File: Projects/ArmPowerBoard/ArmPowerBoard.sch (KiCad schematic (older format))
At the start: 5 parts

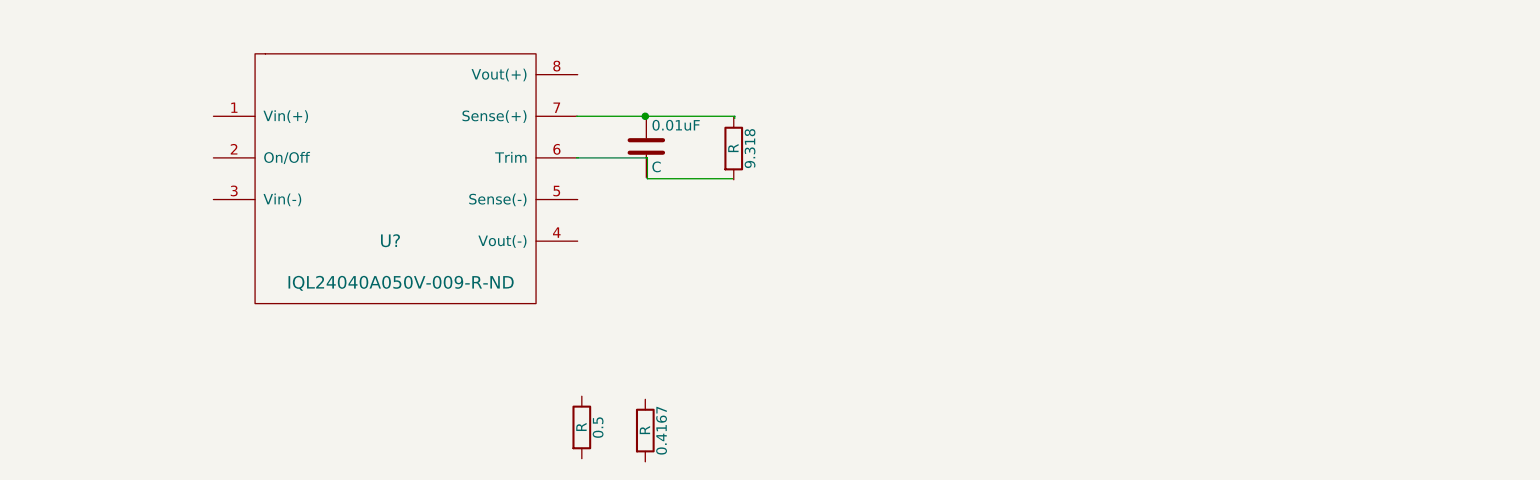
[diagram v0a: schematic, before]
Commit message: Edit Arm power board
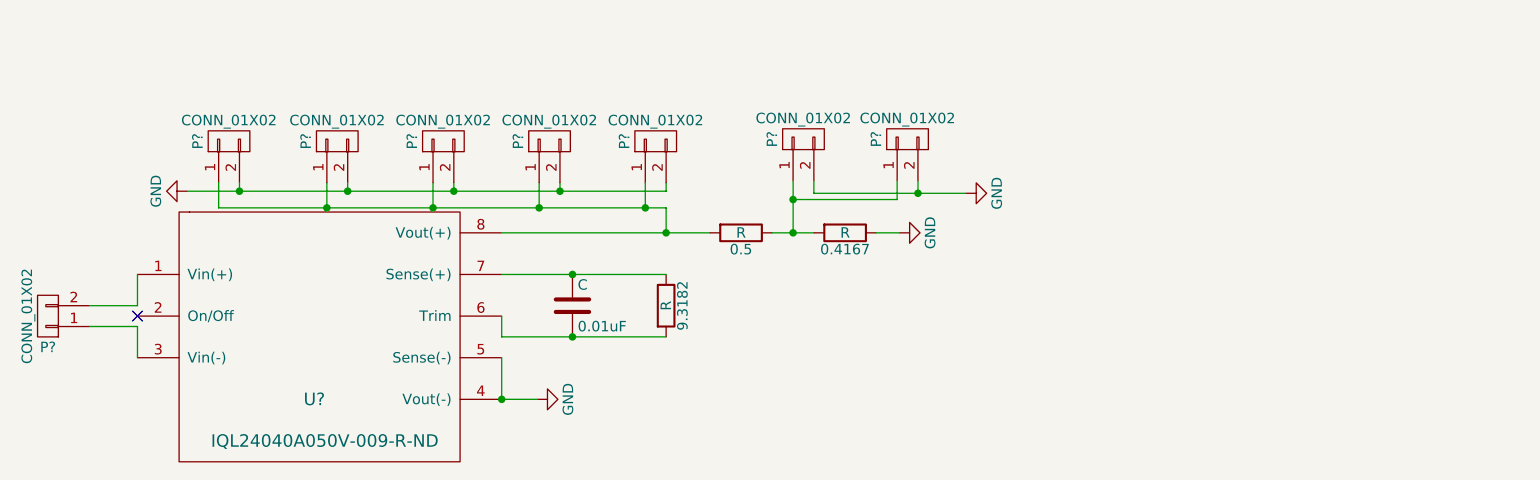
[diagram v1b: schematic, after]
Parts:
- removed 0.01uF: C, symbol C
- removed 9.318: R, symbol R
- removed U?: IQL24040A050V-009-R-ND, symbol IQL24040A050V-009-R-ND
- added 9.3182: R, symbol R
- added C: 0.01uF, symbol C
- added P? (x8): CONN_01X02, symbol CONN_01X02
- added U?: IQL24040A050V-009-R-ND, symbol IQL24040A050V-009-R-ND
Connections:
- net labels added: GND
- wire segments 6 -> 31
- no-connect marks 0 -> 1

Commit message: did some work on the ArmPowerBoard schematic and layout
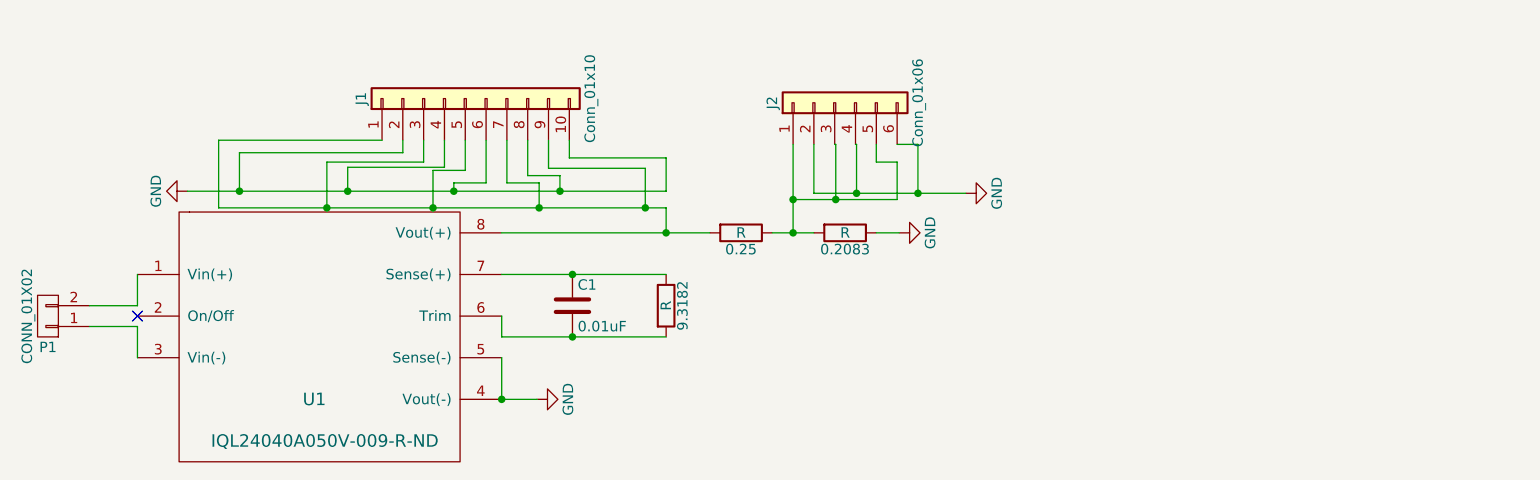
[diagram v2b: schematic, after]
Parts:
- removed P? (x7): CONN_01X02, symbol CONN_01X02
- added J1: Conn_01x10, USST-footprints:Phoenix_Contact_Terminal_Block_1x10_1935242, symbol Conn_01x10
- added J2: Conn_01x06, USST-footprints:TerminalBlock_Pheonix_PT-5mm_6pol, symbol Conn_01x06
- 0.2083: renamed from 0.4167; footprint (none) -> Resistors_SMD:R_1218
- 0.25: renamed from 0.5; footprint (none) -> Resistors_SMD:R_1218
- 9.3182: footprint (none) -> Resistors_SMD:R_1218
- C1: renamed from C; footprint (none) -> Capacitors_SMD:C_1206
- P1: renamed from P?; footprint (none) -> USST-footprints:Phoenix_Contact_1770539
- U1: renamed from U?; footprint (none) -> USST-footprints:IQL24040A050V_Power_Supply
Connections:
- net GND: now also J1.10 (Pin_10), J1.2 (Pin_2), J1.4 (Pin_4), J1.6 (Pin_6), J1.8 (Pin_8), J2.2 (Pin_2), J2.4 (Pin_4), J2.6 (Pin_6)
- net at 0.25.2, U1.8 (Vout(+)): now also J1.1 (Pin_1), J1.3 (Pin_3), J1.5 (Pin_5), J1.7 (Pin_7), J1.9 (Pin_9)
- net at 0.2083.2, 0.25.1: now also J2.1 (Pin_1), J2.3 (Pin_3), J2.5 (Pin_5)
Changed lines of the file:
@@
 LIBS:contrib
 LIBS:valves
-LIBS:USST-parts
 LIBS:ArmPowerBoard-cache
 EELAYER 25 0
@@
 NoConn ~ 3650 3220
 $Comp
-L IQL24040A050V-009-R-ND U?
+L IQL24040A050V-009-R-ND U1
 U 1 1 5AC545D9
 P 4500 3520
-F 0 "U?" H 4500 3420 60  0000 C CNN
+F 0 "U1" H 4500 3420 60  0000 C CNN
 F 1 "IQL24040A050V-009-R-ND" H 4550 3220 60  0000 C CNN
-F 2 "" H 4400 3420 60  0001 C CNN
+F 2 "USST-footprints:IQL24040A050V_Power_Supply" H 4400 3420 60  0001 C CNN
 F 3 "" H 4400 3420 60  0001 C CNN
 	1    4500 3520
@@
 $EndComp
 $Comp
-L C C
+L C C1
 U 1 1 5AC54A7E
 P 5740 3170
-F 0 "C" H 5765 3270 50  0000 L CNN
+F 0 "C1" H 5765 3270 50  0000 L CNN
 F 1 "0.01uF" H 5765 3070 50  0000 L CNN
-F 2 "" H 5778 3020 50  0000 C CNN
+F 2 "Capacitors_SMD:C_1206" H 5778 3020 50  0001 C CNN
 F 3 "" H 5740 3170 50  0000 C CNN
 	1    5740 3170
@@
 F 0 "9.3182" V 6270 3170 50  0000 C CNN
 F 1 "R" V 6190 3170 50  0000 C CNN
-F 2 "" V 6120 3170 50  0000 C CNN
+F 2 "Resistors_SMD:R_1218" V 6120 3170 50  0001 C CNN
 F 3 "" H 6190 3170 50  0000 C CNN
 	1    6190 3170
@@
 $EndComp
 $Comp
-L R 0.4167
+L R 0.2083
 U 1 1 5AC54C78
 P 7050 2820
-F 0 "0.4167" V 7130 2820 50  0000 C CNN
+F 0 "0.2083" V 7130 2820 50  0000 C CNN
 F 1 "R" V 7050 2820 50  0000 C CNN
-F 2 "" V 6980 2820 50  0000 C CNN
+F 2 "Resistors_SMD:R_1218" V 6980 2820 50  0001 C CNN
 F 3 "" H 7050 2820 50  0000 C CNN
 	1    7050 2820
@@
 $EndComp
 $Comp
-L R 0.5
+L R 0.25
 U 1 1 5AC54CA5
 P 6550 2820
-F 0 "0.5" V 6630 2820 50  0000 C CNN
+F 0 "0.25" V 6630 2820 50  0000 C CNN
 F 1 "R" V 6550 2820 50  0000 C CNN
-F 2 "" V 6480 2820 50  0000 C CNN
+F 2 "Resistors_SMD:R_1218" V 6480 2820 50  0001 C CNN
 F 3 "" H 6550 2820 50  0000 C CNN
 	1    6550 2820
@@
 $EndComp
 $Comp
-L GND #PWR?
+L GND #PWR01
 U 1 1 5AC54E0F
 P 7310 2820
-F 0 "#PWR?" H 7310 2570 50  0001 C CNN
+F 0 "#PWR01" H 7310 2570 50  0001 C CNN
 F 1 "GND" H 7310 2670 50  0000 C CNN
 F 2 "" H 7310 2820 50  0000 C CNN
@@
 $EndComp
 $Comp
-L GND #PWR?
+L GND #PWR02
 U 1 1 5AC55060
 P 5570 3620
-F 0 "#PWR?" H 5570 3370 50  0001 C CNN
+F 0 "#PWR02" H 5570 3370 50  0001 C CNN
 F 1 "GND" H 5570 3470 50  0000 C CNN
 F 2 "" H 5570 3620 50  0000 C CNN
@@
 $EndComp
 $Comp
-L CONN_01X02 P?
+L CONN_01X02 P1
 U 1 1 5AC864F2
 P 3220 3220
-F 0 "P?" H 3220 3370 50  0000 C CNN
+F 0 "P1" H 3220 3370 50  0000 C CNN
 F 1 "CONN_01X02" V 3320 3220 50  0000 C CNN
-F 2 "" H 3220 3220 50  0000 C CNN
+F 2 "USST-footprints:Phoenix_Contact_1770539" H 3220 3220 50  0001 C CNN
 F 3 "" H 3220 3220 50  0000 C CNN
 	1    3220 3220
@@
 $EndComp
 $Comp
-L CONN_01X02 P?
-U 1 1 5AC86753
-P 6140 2380
-F 0 "P?" H 6140 2530 50  0000 C CNN
-F 1 "CONN_01X02" V 6240 2380 50  0000 C CNN
-F 2 "" H 6140 2380 50  0000 C CNN
-F 3 "" H 6140 2380 50  0000 C CNN
-	1    6140 2380
-	0    -1   -1   0
-$EndComp
-$Comp
-L CONN_01X02 P?
-U 1 1 5AC867AF
-P 5630 2380
-F 0 "P?" H 5630 2530 50  0000 C CNN
-F 1 "CONN_01X02" V 5730 2380 50  0000 C CNN
-F 2 "" H 5630 2380 50  0000 C CNN
-F 3 "" H 5630 2380 50  0000 C CNN
-	1    5630 2380
-	0    -1   -1   0
-$EndComp
-$Comp
-L CONN_01X02 P?
-U 1 1 5AC867D8
-P 5120 2380
-F 0 "P?" H 5120 2530 50  0000 C CNN
-F 1 "CONN_01X02" V 5220 2380 50  0000 C CNN
-F 2 "" H 5120 2380 50  0000 C CNN
-F 3 "" H 5120 2380 50  0000 C CNN
-	1    5120 2380
-	0    -1   -1   0
-$EndComp
-$Comp
-L CONN_01X02 P?
-U 1 1 5AC86811
-P 4610 2380
-F 0 "P?" H 4610 2530 50  0000 C CNN
-F 1 "CONN_01X02" V 4710 2380 50  0000 C CNN
-F 2 "" H 4610 2380 50  0000 C CNN
-F 3 "" H 4610 2380 50  0000 C CNN
-	1    4610 2380
-	0    -1   -1   0
-$EndComp
-$Comp
-L CONN_01X02 P?
-U 1 1 5AC86844
-P 4090 2380
-F 0 "P?" H 4090 2530 50  0000 C CNN
-F 1 "CONN_01X02" V 4190 2380 50  0000 C CNN
-F 2 "" H 4090 2380 50  0000 C CNN
-F 3 "" H 4090 2380 50  0000 C CNN
-	1    4090 2380
-	0    -1   -1   0
-$EndComp
-$Comp
-L GND #PWR?
+L GND #PWR03
 U 1 1 5AC86D1C
 P 3890 2620
-F 0 "#PWR?" H 3890 2370 50  0001 C CNN
+F 0 "#PWR03" H 3890 2370 50  0001 C CNN
 F 1 "GND" H 3890 2470 50  0000 C CNN
 F 2 "" H 3890 2620 50  0000 C CNN
@@
 	0    1    1    0
 $EndComp
-Wire Wire Line
-	6190 3020 5400 3020
-Wire Wire Line
-	5400 3220 5400 3320
-Wire Wire Line
-	5400 3320 6190 3320
-Connection ~ 5740 3020
-Connection ~ 5740 3320
-Wire Wire Line
-	5400 2820 6400 2820
-Wire Wire Line
-	6700 2820 6900 2820
-Wire Wire Line
-	7200 2820 7310 2820
-Connection ~ 6190 2820
-Wire Wire Line
-	6800 2570 6800 2820
-Connection ~ 6800 2820
-Wire Wire Line
-	5400 3420 5400 3620
-Wire Wire Line
-	5390 3620 5570 3620
-Connection ~ 5400 3620
-Wire Wire Line
-	3650 3170 3650 3020
-Wire Wire Line
-	3420 3170 3650 3170
-Wire Wire Line
-	3420 3270 3650 3270
-Wire Wire Line
-	3650 3270 3650 3420
-Wire Wire Line
-	6190 2620 6190 2580
-Wire Wire Line
-	3890 2620 6190 2620
-Wire Wire Line
-	4660 2580 4660 2620
-Connection ~ 4660 2620
-Wire Wire Line
-	4140 2580 4140 2620
-Connection ~ 4140 2620
-Wire Wire Line
-	5170 2580 5170 2620
-Connection ~ 5170 2620
-Wire Wire Line
-	5680 2580 5680 2620
-Connection ~ 5680 2620
-Wire Wire Line
-	4040 2580 4040 2700
-Wire Wire Line
-	4040 2700 6190 2700
-Wire Wire Line
-	6190 2700 6190 2820
-Wire Wire Line
-	4560 2580 4560 2700
-Connection ~ 4560 2700
-Wire Wire Line
-	5070 2580 5070 2700
-Connection ~ 5070 2700
-Wire Wire Line
-	5580 2580 5580 2700
-Connection ~ 5580 2700
-Wire Wire Line
-	6090 2580 6090 2700
-Connection ~ 6090 2700
-$Comp
-L CONN_01X02 P?
-U 1 1 5AC879B1
-P 6850 2370
-F 0 "P?" H 6850 2520 50  0000 C CNN
-F 1 "CONN_01X02" V 6950 2370 50  0000 C CNN
-F 2 "" H 6850 2370 50  0000 C CNN
-F 3 "" H 6850 2370 50  0000 C CNN
-	1    6850 2370
-	0    -1   -1   0
-$EndComp
-$Comp
-L CONN_01X02 P?
-U 1 1 5AC879EA
-P 7350 2370
-F 0 "P?" H 7350 2520 50  0000 C CNN
-F 1 "CONN_01X02" V 7450 2370 50  0000 C CNN
-F 2 "" H 7350 2370 50  0000 C CNN
-F 3 "" H 7350 2370 50  0000 C CNN
-	1    7350 2370
-	0    -1   -1   0
-$EndComp
-Wire Wire Line
-	6800 2660 7300 2660
-Wire Wire Line
-	7300 2660 7300 2570
-Connection ~ 6800 2660
-Wire Wire Line
-	6900 2570 6900 2630
-Wire Wire Line
-	6900 2630 7630 2630
-Wire Wire Line
-	7400 2570 7400 2630
-Connection ~ 7400 2630
-$Comp
-L GND #PWR?
+$Comp
+L GND #PWR04
 U 1 1 5AC87C8C
 P 7630 2630
-F 0 "#PWR?" H 7630 2380 50  0001 C CNN
+F 0 "#PWR04" H 7630 2380 50  0001 C CNN
 F 1 "GND" H 7630 2480 50  0000 C CNN
 F 2 "" H 7630 2630 50  0000 C CNN
@@
 	0    -1   -1   0
 $EndComp
+$Comp
+L Conn_01x06 J2
+U 1 1 5AC95135
+P 7000 2195
+F 0 "J2" H 7000 2495 50  0000 C CNN
+F 1 "Conn_01x06" H 7000 1795 50  0000 C CNN
+F 2 "USST-footprints:TerminalBlock_Pheonix_PT-5mm_6pol" H 7000 2195 50  0001 C CNN
+F 3 "" H 7000 2195 50  0001 C CNN
+	1    7000 2195
+	0    -1   -1   0
+$EndComp
+$Comp
+L Conn_01x10 J1
+U 1 1 5AC943C7
+P 5225 2175
+F 0 "J1" H 5225 2675 50  0000 C CNN
+F 1 "Conn_01x10" H 5225 1575 50  0000 C CNN
+F 2 "USST-footprints:Phoenix_Contact_Terminal_Block_1x10_1935242" H 5225 2175 50  0001 C CNN
+F 3 "" H 5225 2175 50  0001 C CNN
+	1    5225 2175
+	0    -1   -1   0
+$EndComp
+Wire Wire Line
+	5625 2510 5625 2375
+Wire Wire Line
+	6090 2510 5625 2510
+Wire Wire Line
+	5525 2545 5525 2375
+Wire Wire Line
+	5680 2545 5525 2545
+Wire Wire Line
+	5425 2580 5425 2375
+Wire Wire Line
+	5580 2580 5425 2580
+Wire Wire Line
+	5325 2580 5325 2375
+Wire Wire Line
+	5170 2580 5325 2580
+Wire Wire Line
+	5225 2520 5225 2375
+Wire Wire Line
+	5070 2520 5225 2520
+Wire Wire Line
+	5125 2505 5125 2375
+Wire Wire Line
+	4660 2505 5125 2505
+Wire Wire Line
+	5025 2480 5025 2375
+Wire Wire Line
+	4560 2480 5025 2480
+Connection ~ 7400 2630
+Wire Wire Line
+	7400 2395 7400 2630
+Wire Wire Line
+	6900 2630 7630 2630
+Wire Wire Line
+	6900 2395 6900 2630
+Connection ~ 6800 2660
+Wire Wire Line
+	7300 2480 7300 2660
+Wire Wire Line
+	7300 2660 6800 2660
+Connection ~ 6090 2700
+Wire Wire Line
+	6090 2510 6090 2700
+Connection ~ 5580 2700
+Wire Wire Line
+	5580 2580 5580 2700
+Connection ~ 5070 2700
+Wire Wire Line
+	5070 2520 5070 2700
+Connection ~ 4560 2700
+Wire Wire Line
+	4560 2480 4560 2700
+Wire Wire Line
+	6190 2700 6190 2820
+Wire Wire Line
+	4040 2700 6190 2700
+Connection ~ 5680 2620
+Wire Wire Line
+	5680 2545 5680 2620
+Connection ~ 5170 2620
+Wire Wire Line
+	5170 2580 5170 2620
+Connection ~ 4140 2620
+Connection ~ 4660 2620
+Wire Wire Line
+	4660 2505 4660 2620
+Wire Wire Line
+	6190 2620 3890 2620
+Wire Wire Line
+	6190 2460 6190 2620
+Wire Wire Line
+	3650 3270 3650 3420
+Wire Wire Line
+	3420 3270 3650 3270
+Wire Wire Line
+	3420 3170 3650 3170
+Wire Wire Line
+	3650 3170 3650 3020
+Wire Wire Line
+	5400 3420 5400 3620
+Connection ~ 6800 2820
+Wire Wire Line
+	6800 2395 6800 2820
+Connection ~ 6190 2820
+Wire Wire Line
+	7200 2820 7310 2820
+Wire Wire Line
+	6700 2820 6900 2820
+Wire Wire Line
+	5400 2820 6400 2820
+Connection ~ 5740 3320
+Connection ~ 5740 3020
+Wire Wire Line
+	5400 3320 6190 3320
+Wire Wire Line
+	5400 3220 5400 3320
+Wire Wire Line
+	6190 3020 5400 3020
+Wire Wire Line
+	6190 2460 5725 2460
+Wire Wire Line
+	5725 2460 5725 2375
+Wire Wire Line
+	7300 2480 7200 2480
+Wire Wire Line
+	7200 2480 7200 2395
+Connection ~ 7005 2660
+Wire Wire Line
+	7005 2660 7005 2395
+Wire Wire Line
+	7005 2395 7000 2395
+Connection ~ 7105 2630
+Wire Wire Line
+	7105 2630 7105 2395
+Wire Wire Line
+	7105 2395 7100 2395
+Wire Wire Line
+	7400 2395 7300 2395
+Wire Wire Line
+	4040 2700 4040 2375
+Wire Wire Line
+	4040 2375 4825 2375
+Wire Wire Line
+	4140 2620 4140 2435
+Wire Wire Line
+	4140 2435 4925 2435
+Wire Wire Line
+	4925 2435 4925 2375
+Connection ~ 5400 3620
+Wire Wire Line
+	5400 3620 5570 3620
 $EndSCHEMATC

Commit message: Made the Arm PCB
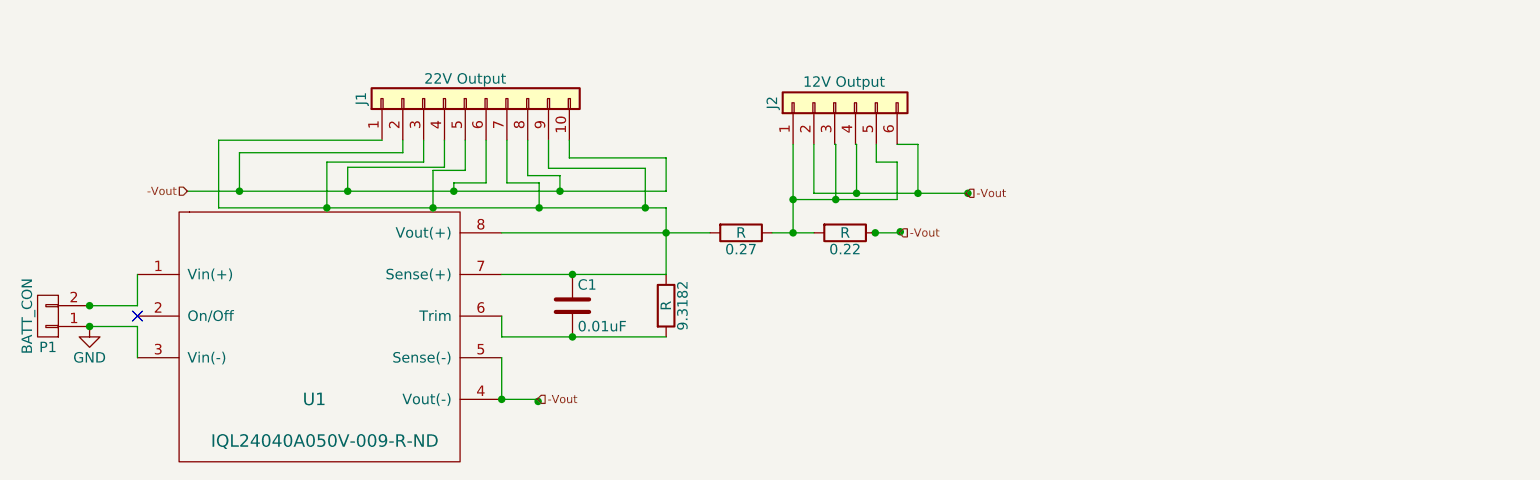
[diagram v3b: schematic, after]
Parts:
- J1: value Conn_01x10 -> 22V Output
- J2: value Conn_01x06 -> 12V Output
- P1: value CONN_01X02 -> BATT_CON
- renumbered 0.2083 to 0.22, 0.25 to 0.27
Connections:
- net GND: now also P1.1 (P1), U1.3 (Vin(-)); no longer 0.22.1, J1.10 (Pin_10), J1.2 (Pin_2), J1.4 (Pin_4), J1.6 (Pin_6), J1.8 (Pin_8), J2.2 (Pin_2), J2.4 (Pin_4), J2.6 (Pin_6), U1.4 (Vout(-)), U1.5 (Sense(-))
- net at 9.3182.1, C1.1, U1.7 (Sense(+)): now also 0.27.2, J1.1 (Pin_1), J1.3 (Pin_3), J1.5 (Pin_5), J1.7 (Pin_7), J1.9 (Pin_9), U1.8 (Vout(+))
- new net -Vout: 0.22.1, J1.10 (Pin_10), J1.2 (Pin_2), J1.4 (Pin_4), J1.6 (Pin_6), J1.8 (Pin_8), J2.2 (Pin_2), J2.4 (Pin_4), J2.6 (Pin_6), U1.4 (Vout(-)), U1.5 (Sense(-))
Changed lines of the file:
@@
 $EndComp
 $Comp
-L R 0.2083
+L R 0.22
 U 1 1 5AC54C78
 P 7050 2820
-F 0 "0.2083" V 7130 2820 50  0000 C CNN
+F 0 "0.22" V 7130 2820 50  0000 C CNN
 F 1 "R" V 7050 2820 50  0000 C CNN
 F 2 "Resistors_SMD:R_1218" V 6980 2820 50  0001 C CNN
@@
 $EndComp
 $Comp
-L R 0.25
+L R 0.27
 U 1 1 5AC54CA5
 P 6550 2820
-F 0 "0.25" V 6630 2820 50  0000 C CNN
+F 0 "0.27" V 6630 2820 50  0000 C CNN
 F 1 "R" V 6550 2820 50  0000 C CNN
 F 2 "Resistors_SMD:R_1218" V 6480 2820 50  0001 C CNN
@@
 $EndComp
 $Comp
-L GND #PWR01
-U 1 1 5AC54E0F
-P 7310 2820
-F 0 "#PWR01" H 7310 2570 50  0001 C CNN
-F 1 "GND" H 7310 2670 50  0000 C CNN
-F 2 "" H 7310 2820 50  0000 C CNN
-F 3 "" H 7310 2820 50  0000 C CNN
-	1    7310 2820
-	0    -1   -1   0
-$EndComp
-$Comp
-L GND #PWR02
-U 1 1 5AC55060
-P 5570 3620
-F 0 "#PWR02" H 5570 3370 50  0001 C CNN
-F 1 "GND" H 5570 3470 50  0000 C CNN
-F 2 "" H 5570 3620 50  0000 C CNN
-F 3 "" H 5570 3620 50  0000 C CNN
-	1    5570 3620
-	0    -1   -1   0
-$EndComp
-$Comp
 L CONN_01X02 P1
 U 1 1 5AC864F2
 P 3220 3220
 F 0 "P1" H 3220 3370 50  0000 C CNN
-F 1 "CONN_01X02" V 3320 3220 50  0000 C CNN
+F 1 "BATT_CON" V 3320 3220 50  0000 C CNN
 F 2 "USST-footprints:Phoenix_Contact_1770539" H 3220 3220 50  0001 C CNN
 F 3 "" H 3220 3220 50  0000 C CNN
@@
 $EndComp
 $Comp
-L GND #PWR03
-U 1 1 5AC86D1C
-P 3890 2620
-F 0 "#PWR03" H 3890 2370 50  0001 C CNN
-F 1 "GND" H 3890 2470 50  0000 C CNN
-F 2 "" H 3890 2620 50  0000 C CNN
-F 3 "" H 3890 2620 50  0000 C CNN
-	1    3890 2620
-	0    1    1    0
-$EndComp
-$Comp
-L GND #PWR04
-U 1 1 5AC87C8C
-P 7630 2630
-F 0 "#PWR04" H 7630 2380 50  0001 C CNN
-F 1 "GND" H 7630 2480 50  0000 C CNN
-F 2 "" H 7630 2630 50  0000 C CNN
-F 3 "" H 7630 2630 50  0000 C CNN
-	1    7630 2630
-	0    -1   -1   0
-$EndComp
-$Comp
 L Conn_01x06 J2
 U 1 1 5AC95135
 P 7000 2195
 F 0 "J2" H 7000 2495 50  0000 C CNN
-F 1 "Conn_01x06" H 7000 1795 50  0000 C CNN
+F 1 "12V Output" V 7100 2150 50  0000 C CNN
 F 2 "USST-footprints:TerminalBlock_Pheonix_PT-5mm_6pol" H 7000 2195 50  0001 C CNN
 F 3 "" H 7000 2195 50  0001 C CNN
@@
 P 5225 2175
 F 0 "J1" H 5225 2675 50  0000 C CNN
-F 1 "Conn_01x10" H 5225 1575 50  0000 C CNN
+F 1 "22V Output" V 5320 2175 50  0000 C CNN
 F 2 "USST-footprints:Phoenix_Contact_Terminal_Block_1x10_1935242" H 5225 2175 50  0001 C CNN
 F 3 "" H 5225 2175 50  0001 C CNN
@@
 Connection ~ 7400 2630
 Wire Wire Line
-	7400 2395 7400 2630
+	7400 2630 7400 2395
 Wire Wire Line
 	6900 2630 7630 2630
@@
 Connection ~ 6800 2660
 Wire Wire Line
-	7300 2480 7300 2660
-Wire Wire Line
-	7300 2660 6800 2660
+	7300 2660 7300 2480
+Wire Wire Line
+	6800 2660 7300 2660
 Connection ~ 6090 2700
 Wire Wire Line
-	6090 2510 6090 2700
+	6090 2700 6090 2510
 Connection ~ 5580 2700
 Wire Wire Line
-	5580 2580 5580 2700
+	5580 2700 5580 2580
 Connection ~ 5070 2700
 Wire Wire Line
-	5070 2520 5070 2700
+	5070 2700 5070 2520
 Connection ~ 4560 2700
 Wire Wire Line
 	4560 2480 4560 2700
 Wire Wire Line
-	6190 2700 6190 2820
+	6190 2700 6190 3020
 Wire Wire Line
 	4040 2700 6190 2700
@@
 	4660 2505 4660 2620
 Wire Wire Line
-	6190 2620 3890 2620
-Wire Wire Line
-	6190 2460 6190 2620
+	3890 2620 6190 2620
+Wire Wire Line
+	6190 2620 6190 2460
 Wire Wire Line
 	3650 3270 3650 3420
@@
 Wire Wire Line
 	6800 2395 6800 2820
-Connection ~ 6190 2820
 Wire Wire Line
 	7200 2820 7310 2820
@@
 Wire Wire Line
 	5400 3620 5570 3620
+$Comp
+L GND #PWR01
+U 1 1 5AE0D3FF
+P 3420 3270
+F 0 "#PWR01" H 3420 3020 50  0001 C CNN
+F 1 "GND" H 3420 3120 50  0000 C CNN
+F 2 "" H 3420 3270 50  0000 C CNN
+F 3 "" H 3420 3270 50  0000 C CNN
+	1    3420 3270
+	1    0    0    -1
+$EndComp
+Text HLabel 5570 3620 2    39   Input ~ 0
+-Vout
+Text HLabel 7310 2820 2    39   Input ~ 0
+-Vout
+Text HLabel 7630 2630 2    39   Input ~ 0
+-Vout
+Text HLabel 3890 2620 0    39   Input ~ 0
+-Vout
+Connection ~ 5575 3630
+Connection ~ 7195 2820
+Connection ~ 7640 2630
+Connection ~ 7315 2815
+Connection ~ 3420 3170
+Connection ~ 3420 3270
+Connection ~ 6190 2820
 $EndSCHEMATC
